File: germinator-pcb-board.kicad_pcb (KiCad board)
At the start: 2 copper layers, 72.1 x 52.1 mm, 12 parts, among them J1 Conn_01x15_Socket, J2 Conn_01x15_Socket, J3 Screw_Terminal_01x04, J4 Screw_Terminal_01x03, J5 Screw_Terminal_01x03, J6 Screw_Terminal_01x03, J7 Screw_Terminal_01x03, U1 ESP32-DEVKIT-V1

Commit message: Layout step 7: export gerber files
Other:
- board text added: "0.2000 mm / 0.0000 mm"
- board text added: "0.3000 mm"
- board text added: "1.6000 mm"
- board text added: "2"
- board text added: "72.1360 mm x 52.0700 mm"
- board text added: "BOARD CHARACTERISTICS"
- board text added: "Board Thickness:"
- board text added: "Board overall dimensions:"
- board text added: "Castellated pads:"
- board text added: "Copper Finish:"
- board text added: "Copper Layer Count:"
- board text added: "Edge card connectors:"
- board text added: "Impedance Control:"
- board text added: "Min hole diameter:"
- board text added: "Min track/spacing:"
- board text added: "No"
- board text added: "None"
- board text added: "Plated Board Edge:"

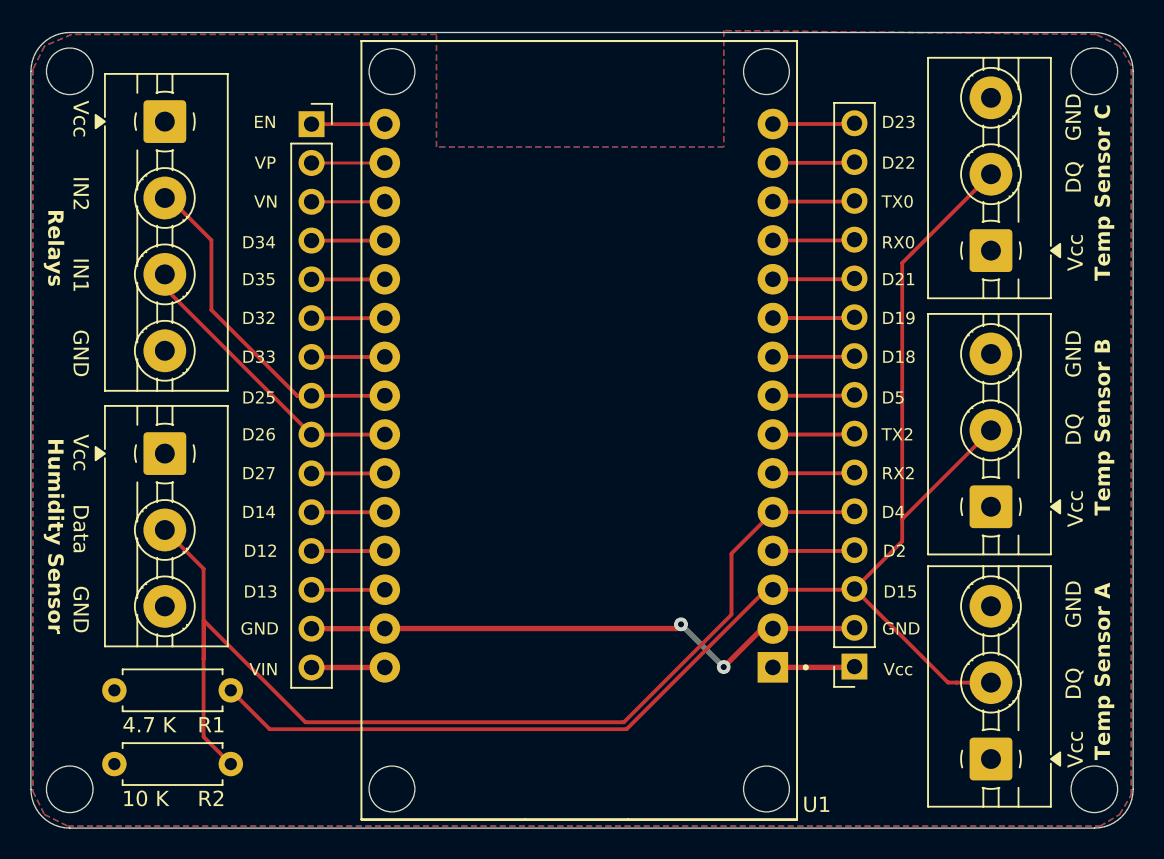
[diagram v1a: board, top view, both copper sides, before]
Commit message: adding terminal blocks 3d models and making traces wider
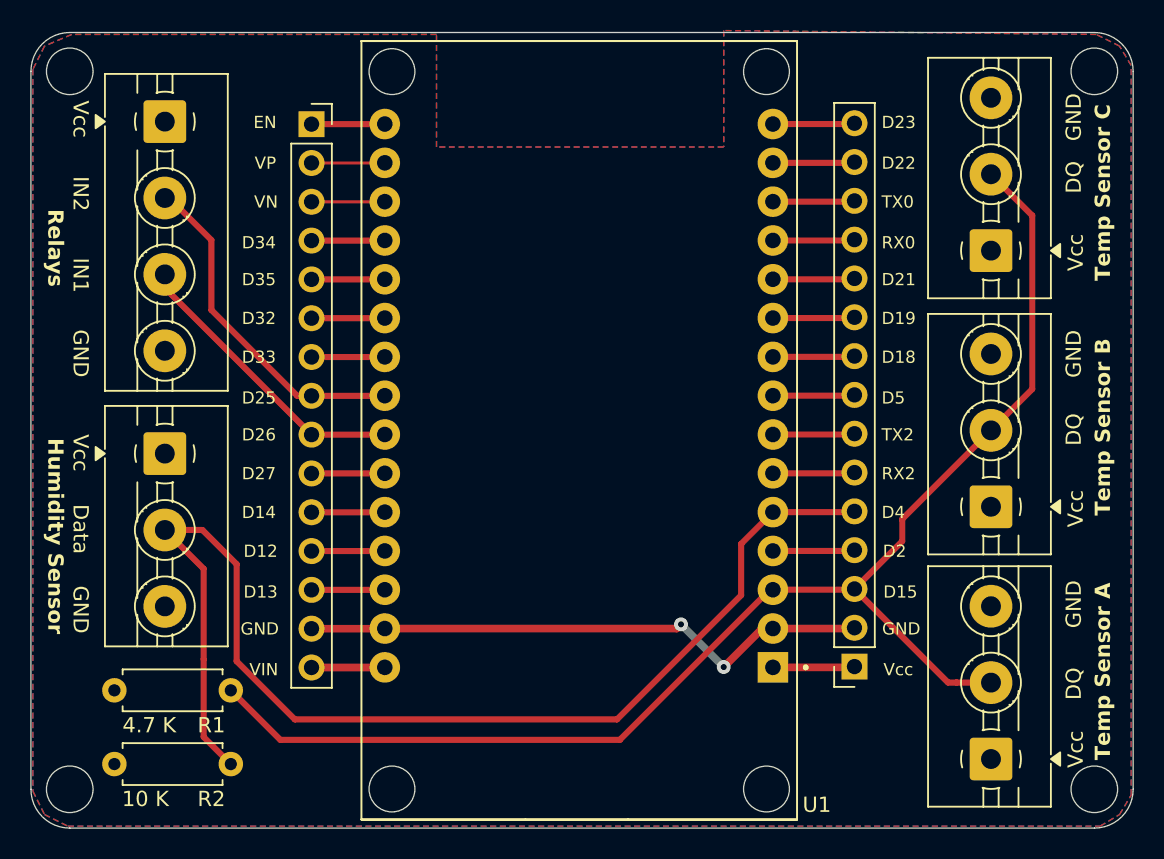
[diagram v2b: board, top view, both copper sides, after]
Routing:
- net /D4: track 73.1 -> 78.7 mm
- net /D15: track 96.2 -> 90.8 mm
